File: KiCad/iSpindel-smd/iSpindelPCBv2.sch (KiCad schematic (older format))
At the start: 21 parts, among them J1 PROG, J2 PROG_con, SW1 SW_DPDT_x2, U1 MIC5219-3.3, U2 GY-521, U3 TP4056-shield-6PIN, U4 DS18B20, U5 LoRa_Ra-02, U6 ESP-07S

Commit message: small fix
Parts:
- added SW?: SW_DPDT_x2, KiCadCustomLibs:SK12D07VG3, symbol SW_DPDT_x2
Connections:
- net VCC: now also SW?.1 (A)
- net at SW1.2 (B), U3.3 (OUT+): now also SW?.2 (B)
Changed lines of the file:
@@
 Wire Wire Line
 	10600 1600 10450 1600
+$Comp
+L SW_DPDT_x2 SW?
+U 1 1 5B55F055
+P 8850 4650
+F 0 "SW?" H 8850 4820 50  0000 C CNN
+F 1 "SW_DPDT_x2" H 8850 4450 50  0000 C CNN
+F 2 "KiCadCustomLibs:SK12D07VG3" H 8850 4650 50  0001 C CNN
+F 3 "" H 8850 4650 50  0001 C CNN
+	1    8850 4650
+	1    0    0    -1
+$EndComp
+Wire Wire Line
+	8650 4650 8500 4650
+Wire Wire Line
+	8500 4650 8500 4100
+Connection ~ 8500 4100
+$Comp
+L VCC #PWR?
+U 1 1 5B55F1C0
+P 9050 4550
+F 0 "#PWR?" H 9050 4400 50  0001 C CNN
+F 1 "VCC" H 9050 4700 50  0000 C CNN
+F 2 "" H 9050 4550 50  0001 C CNN
+F 3 "" H 9050 4550 50  0001 C CNN
+	1    9050 4550
+	1    0    0    -1
+$EndComp
 $EndSCHEMATC

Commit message: Some work still in progress
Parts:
- removed SW1, SW?: SW_DPDT_x2, KiCadCustomLibs:SK12D07VG3, symbol SW_DPDT_x2
- added SW1: SW_SPDT, KiCadCustomLibs:SK12D07VG3, symbol SW_SPDT
- D1: footprint (none) -> Diodes_SMD:D_SOD-523
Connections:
- net VCC: now also SW1.2 (B); no longer J2.4 (Pin_4)
- net at U3.3 (OUT+): now also SW1.3 (C)
- new net VCC_PROG: J2.4 (Pin_4), SW1.1 (A)
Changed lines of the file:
@@
-$EndComp
-$Comp
-L SW_DPDT_x2 SW1
-U 1 1 5B533766
-P 8850 4100
-F 0 "SW1" H 8850 4270 50  0000 C CNN
-F 1 "SW_DPDT_x2" H 8850 3900 50  0000 C CNN
-F 2 "KiCadCustomLibs:SK12D07VG3" H 8850 4100 50  0001 C CNN
-F 3 "" H 8850 4100 50  0001 C CNN
-	1    8850 4100
-	1    0    0    -1
 $EndComp
 $Comp
@@
 	1    0    0    -1
 $EndComp
-Wire Wire Line
-	7850 4100 8650 4100
 NoConn ~ 6850 4100
 NoConn ~ 7850 4600
@@
 F 0 "D1" H 7750 2280 50  0000 L CNN
 F 1 "Schottky" H 7600 2350 50  0000 L CNN
-F 2 "" V 7800 2200 50  0001 C CNN
+F 2 "Diodes_SMD:D_SOD-523" V 7800 2200 50  0001 C CNN
 F 3 "" V 7800 2200 50  0001 C CNN
 	1    7800 2200
@@
 	10150 1700 10600 1700
 $Comp
-L VCC #PWR28
-U 1 1 5B54DB80
-P 10450 1600
-F 0 "#PWR28" H 10450 1450 50  0001 C CNN
-F 1 "VCC" H 10450 1750 50  0000 C CNN
-F 2 "" H 10450 1600 50  0001 C CNN
-F 3 "" H 10450 1600 50  0001 C CNN
-	1    10450 1600
-	1    0    0    -1
-$EndComp
-Wire Wire Line
-	10600 1600 10450 1600
-$Comp
-L SW_DPDT_x2 SW?
-U 1 1 5B55F055
-P 8850 4650
-F 0 "SW?" H 8850 4820 50  0000 C CNN
-F 1 "SW_DPDT_x2" H 8850 4450 50  0000 C CNN
-F 2 "KiCadCustomLibs:SK12D07VG3" H 8850 4650 50  0001 C CNN
-F 3 "" H 8850 4650 50  0001 C CNN
-	1    8850 4650
-	1    0    0    -1
-$EndComp
-Wire Wire Line
-	8650 4650 8500 4650
-Wire Wire Line
-	8500 4650 8500 4100
-Connection ~ 8500 4100
-$Comp
-L VCC #PWR?
-U 1 1 5B55F1C0
-P 9050 4550
-F 0 "#PWR?" H 9050 4400 50  0001 C CNN
-F 1 "VCC" H 9050 4700 50  0000 C CNN
-F 2 "" H 9050 4550 50  0001 C CNN
-F 3 "" H 9050 4550 50  0001 C CNN
-	1    9050 4550
-	1    0    0    -1
-$EndComp
+L SW_SPDT SW1
+U 1 1 5B570E68
+P 8850 4000
+F 0 "SW1" H 8850 4170 50  0000 C CNN
+F 1 "SW_SPDT" H 8850 3800 50  0000 C CNN
+F 2 "KiCadCustomLibs:SK12D07VG3" H 8850 4000 50  0001 C CNN
+F 3 "" H 8850 4000 50  0001 C CNN
+	1    8850 4000
+	-1   0    0    1
+$EndComp
+Text Label 8200 4100 0    60   ~ 0
+VCC_PROG
+Wire Wire Line
+	10600 1600 10150 1600
+Text Label 10150 1600 0    60   ~ 0
+VCC_PROG
+Wire Wire Line
+	7850 4100 7900 4100
+Wire Wire Line
+	7900 4100 7900 3900
+Wire Wire Line
+	7900 3900 8650 3900
+Wire Wire Line
+	8650 4100 8200 4100
 $EndSCHEMATC

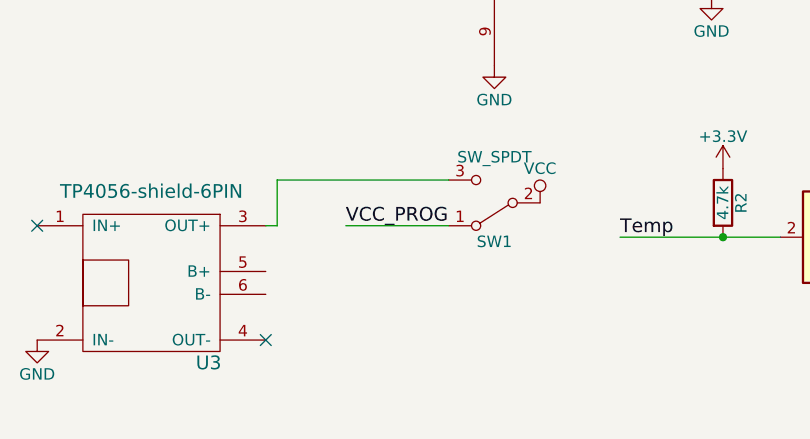
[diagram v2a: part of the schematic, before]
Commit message: Add TH variant
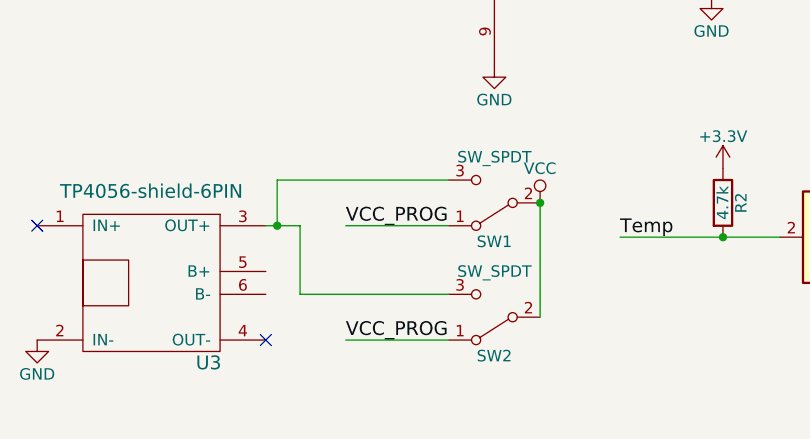
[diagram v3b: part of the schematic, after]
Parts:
- added SW2: SW_SPDT, KiCadCustomLibs:SS-12F23, symbol SW_SPDT
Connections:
- net VCC: now also SW2.2 (B)
- net VCC_PROG: now also SW2.1 (A)
- net at SW1.3 (C), U3.3 (OUT+): now also SW2.3 (C)
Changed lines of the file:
@@
 $EndComp
 $Comp
-L GND #PWR29
+L GND #PWR28
 U 1 1 5B54D95D
 P 10600 1900
-F 0 "#PWR29" H 10600 1650 50  0001 C CNN
+F 0 "#PWR28" H 10600 1650 50  0001 C CNN
 F 1 "GND" H 10600 1750 50  0000 C CNN
 F 2 "" H 10600 1900 50  0001 C CNN
@@
 VCC_PROG
 Wire Wire Line
-	7850 4100 7900 4100
+	7850 4100 8000 4100
 Wire Wire Line
 	7900 4100 7900 3900
@@
 Wire Wire Line
 	8650 4100 8200 4100
+$Comp
+L SW_SPDT SW2
+U 1 1 5B585D1D
+P 8850 4500
+F 0 "SW2" H 8850 4670 50  0000 C CNN
+F 1 "SW_SPDT" H 8850 4300 50  0000 C CNN
+F 2 "KiCadCustomLibs:SS-12F23" H 8850 4500 50  0001 C CNN
+F 3 "" H 8850 4500 50  0001 C CNN
+	1    8850 4500
+	-1   0    0    1
+$EndComp
+Wire Wire Line
+	9050 4000 9050 4500
+Connection ~ 9050 4000
+Wire Wire Line
+	8650 4400 8000 4400
+Wire Wire Line
+	8000 4400 8000 4100
+Connection ~ 7900 4100
+Wire Wire Line
+	8650 4600 8200 4600
+Text Label 8200 4600 0    60   ~ 0
+VCC_PROG
 $EndSCHEMATC

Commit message: Add led
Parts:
- added C6: 100n, Capacitors_SMD:C_0603, symbol C
- added D2: LED, LEDs:LED_0805, symbol LED
- added R7: 4.7k, Resistors_SMD:R_0603, symbol R
- added SW3: SW_Push, KiCadCustomLibs:Button_TS-018, symbol SW_Push
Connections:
- net +3V3: now also R7.1
- net GND: now also C6.2, SW3.2
- net at D1.2 (A), R5.2, U6.1 (REST): now also C6.1, SW3.1
- net LED: now reaches U6.13 (GPIO4)
- net LED: now also D2.1 (K)
- new net: D2.2 (A), R7.2
- no-connect marks 13 -> 12
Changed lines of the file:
@@
 	9400 4150 10100 4150
 $Comp
-L +3.3V #PWR25
+L +3.3V #PWR27
 U 1 1 5B5302EE
 P 9850 3850
-F 0 "#PWR25" H 9850 3700 50  0001 C CNN
+F 0 "#PWR27" H 9850 3700 50  0001 C CNN
 F 1 "+3.3V" H 9850 3990 50  0000 C CNN
 F 2 "" H 9850 3850 50  0001 C CNN
@@
 Connection ~ 9850 4150
 $Comp
-L GND #PWR27
+L GND #PWR29
 U 1 1 5B530B26
 P 10400 4450
-F 0 "#PWR27" H 10400 4200 50  0001 C CNN
+F 0 "#PWR29" H 10400 4200 50  0001 C CNN
 F 1 "GND" H 10400 4300 50  0000 C CNN
 F 2 "" H 10400 4450 50  0001 C CNN
@@
 $EndComp
 $Comp
-L VCC #PWR22
+L VCC #PWR24
 U 1 1 5B53B586
 P 9050 4000
-F 0 "#PWR22" H 9050 3850 50  0001 C CNN
+F 0 "#PWR24" H 9050 3850 50  0001 C CNN
 F 1 "VCC" H 9050 4150 50  0000 C CNN
 F 2 "" H 9050 4000 50  0001 C CNN
@@
 $EndComp
 $Comp
-L VCC #PWR26
+L VCC #PWR28
 U 1 1 5B53B686
 P 10400 3850
-F 0 "#PWR26" H 10400 3700 50  0001 C CNN
+F 0 "#PWR28" H 10400 3700 50  0001 C CNN
 F 1 "VCC" H 10400 4000 50  0000 C CNN
 F 2 "" H 10400 3850 50  0001 C CNN
@@
 	7450 2300 7950 2300
 $Comp
-L GND #PWR16
+L GND #PWR17
 U 1 1 5B542A93
 P 7450 2600
-F 0 "#PWR16" H 7450 2350 50  0001 C CNN
+F 0 "#PWR17" H 7450 2350 50  0001 C CNN
 F 1 "GND" H 7450 2450 50  0000 C CNN
 F 2 "" H 7450 2600 50  0001 C CNN
@@
 $EndComp
 $Comp
-L VCC #PWR15
+L VCC #PWR16
 U 1 1 5B542B16
 P 7450 2000
-F 0 "#PWR15" H 7450 1850 50  0001 C CNN
+F 0 "#PWR16" H 7450 1850 50  0001 C CNN
 F 1 "VCC" H 7450 2150 50  0000 C CNN
 F 2 "" H 7450 2000 50  0001 C CNN
@@
 Connection ~ 7450 2300
 $Comp
-L +3.3V #PWR20
+L +3.3V #PWR22
 U 1 1 5B542EA1
 P 8850 1600
-F 0 "#PWR20" H 8850 1450 50  0001 C CNN
+F 0 "#PWR22" H 8850 1450 50  0001 C CNN
 F 1 "+3.3V" H 8850 1740 50  0000 C CNN
 F 2 "" H 8850 1600 50  0001 C CNN
@@
 $EndComp
 $Comp
-L GND #PWR21
+L GND #PWR23
 U 1 1 5B54787D
 P 8850 3400
-F 0 "#PWR21" H 8850 3150 50  0001 C CNN
+F 0 "#PWR23" H 8850 3150 50  0001 C CNN
 F 1 "GND" H 8850 3250 50  0000 C CNN
 F 2 "" H 8850 3400 50  0001 C CNN
@@
 P 7800 2200
 F 0 "D1" H 7750 2280 50  0000 L CNN
-F 1 "Schottky" H 7600 2350 50  0000 L CNN
+F 1 "Schottky" H 7550 2350 50  0001 L CNN
 F 2 "Diodes_SMD:D_SOD-523" V 7800 2200 50  0001 C CNN
 F 3 "" V 7800 2200 50  0001 C CNN
@@
 Text Label 7650 2600 0    60   ~ 0
 SCK
-NoConn ~ 9750 2500
 Wire Wire Line
 	7950 2400 7800 2400
@@
 $EndComp
 $Comp
-L +3.3V #PWR17
+L +3.3V #PWR19
 U 1 1 5B548D3F
 P 7950 1750
-F 0 "#PWR17" H 7950 1600 50  0001 C CNN
+F 0 "#PWR19" H 7950 1600 50  0001 C CNN
 F 1 "+3.3V" H 7950 1890 50  0000 C CNN
 F 2 "" H 7950 1750 50  0001 C CNN
@@
 Connection ~ 9800 2800
 $Comp
-L GND #PWR23
+L GND #PWR25
 U 1 1 5B549B49
 P 9800 3100
-F 0 "#PWR23" H 9800 2850 50  0001 C CNN
+F 0 "#PWR25" H 9800 2850 50  0001 C CNN
 F 1 "GND" H 9800 2950 50  0000 C CNN
 F 2 "" H 9800 3100 50  0001 C CNN
@@
 	8250 1250 8500 1250
 $Comp
-L +3.3V #PWR18
+L +3.3V #PWR20
 U 1 1 5B54A171
 P 8400 1250
-F 0 "#PWR18" H 8400 1100 50  0001 C CNN
+F 0 "#PWR20" H 8400 1100 50  0001 C CNN
 F 1 "+3.3V" H 8400 1390 50  0000 C CNN
 F 2 "" H 8400 1250 50  0001 C CNN
@@
 Connection ~ 8400 1250
 $Comp
-L GND #PWR19
+L GND #PWR21
 U 1 1 5B54A232
 P 8400 1550
-F 0 "#PWR19" H 8400 1300 50  0001 C CNN
+F 0 "#PWR21" H 8400 1300 50  0001 C CNN
 F 1 "GND" H 8400 1400 50  0000 C CNN
 F 2 "" H 8400 1550 50  0001 C CNN
@@
 SDA
 $Comp
-L GND #PWR24
+L GND #PWR26
 U 1 1 5B54AE12
 P 9850 1550
-F 0 "#PWR24" H 9850 1300 50  0001 C CNN
+F 0 "#PWR26" H 9850 1300 50  0001 C CNN
 F 1 "GND" H 9850 1400 50  0000 C CNN
 F 2 "" H 9850 1550 50  0001 C CNN
@@
 $EndComp
 $Comp
-L GND #PWR28
+L GND #PWR30
 U 1 1 5B54D95D
 P 10600 1900
-F 0 "#PWR28" H 10600 1650 50  0001 C CNN
+F 0 "#PWR30" H 10600 1650 50  0001 C CNN
 F 1 "GND" H 10600 1750 50  0000 C CNN
 F 2 "" H 10600 1900 50  0001 C CNN
@@
 Text Label 8200 4600 0    60   ~ 0
 VCC_PROG
+$Comp
+L SW_Push SW3
+U 1 1 5B5AFB9B
+P 7350 1600
+F 0 "SW3" H 7400 1700 50  0000 L CNN
+F 1 "SW_Push" H 7350 1540 50  0000 C CNN
+F 2 "KiCadCustomLibs:Button_TS-018" H 7350 1800 50  0001 C CNN
+F 3 "" H 7350 1800 50  0001 C CNN
+	1    7350 1600
+	-1   0    0    -1
+$EndComp
+Wire Wire Line
+	7550 1600 7750 1600
+Wire Wire Line
+	7750 1600 7750 2050
+Wire Wire Line
+	7750 2050 7950 2050
+Connection ~ 7950 2050
+$Comp
+L GND #PWR15
+U 1 1 5B5AFCF8
+P 7150 1700
+F 0 "#PWR15" H 7150 1450 50  0001 C CNN
+F 1 "GND" H 7150 1550 50  0000 C CNN
+F 2 "" H 7150 1700 50  0001 C CNN
+F 3 "" H 7150 1700 50  0001 C CNN
+	1    7150 1700
+	1    0    0    -1
+$EndComp
+Wire Wire Line
+	7150 1600 7150 1700
+$Comp
+L C C6
+U 1 1 5B5B067E
+P 7600 1750
+F 0 "C6" H 7625 1850 50  0000 L CNN
+F 1 "100n" H 7600 1950 50  0000 L CNN
+F 2 "Capacitors_SMD:C_0603" H 7638 1600 50  0001 C CNN
+F 3 "" H 7600 1750 50  0001 C CNN
+	1    7600 1750
+	1    0    0    -1
+$EndComp
+Connection ~ 7600 1600
+$Comp
+L GND #PWR18
+U 1 1 5B5B0740
+P 7600 1900
+F 0 "#PWR18" H 7600 1650 50  0001 C CNN
+F 1 "GND" H 7600 1750 50  0000 C CNN
+F 2 "" H 7600 1900 50  0001 C CNN
+F 3 "" H 7600 1900 50  0001 C CNN
+	1    7600 1900
+	1    0    0    -1
+$EndComp
+Wire Wire Line
+	9750 2500 10050 2500
+Text Label 10050 2500 2    60   ~ 0
+LED
+$Comp
+L LED D2
+U 1 1 5B5B3D9A
+P 10400 3150
+F 0 "D2" H 10400 3250 50  0000 C CNN
+F 1 "LED" H 10400 3050 50  0000 C CNN
+F 2 "LEDs:LED_0805" H 10400 3150 50  0001 C CNN
+F 3 "" H 10400 3150 50  0001 C CNN
+	1    10400 3150
+	1    0    0    -1
+$EndComp
+$Comp
+L R R7
+U 1 1 5B5B4294
+P 10700 3150
+F 0 "R7" V 10780 3150 50  0000 C CNN
+F 1 "4.7k" V 10700 3150 50  0000 C CNN
+F 2 "Resistors_SMD:R_0603" V 10630 3150 50  0001 C CNN
+F 3 "" H 10700 3150 50  0001 C CNN
+	1    10700 3150
+	0    1    1    0
+$EndComp
+$Comp
+L +3.3V #PWR31
+U 1 1 5B5B4324
+P 10850 3150
+F 0 "#PWR31" H 10850 3000 50  0001 C CNN
+F 1 "+3.3V" H 10850 3290 50  0000 C CNN
+F 2 "" H 10850 3150 50  0001 C CNN
+F 3 "" H 10850 3150 50  0001 C CNN
+	1    10850 3150
+	1    0    0    -1
+$EndComp
+Wire Wire Line
+	10250 3150 10000 3150
+Text Label 10000 3150 0    60   ~ 0
+LED
 $EndSCHEMATC

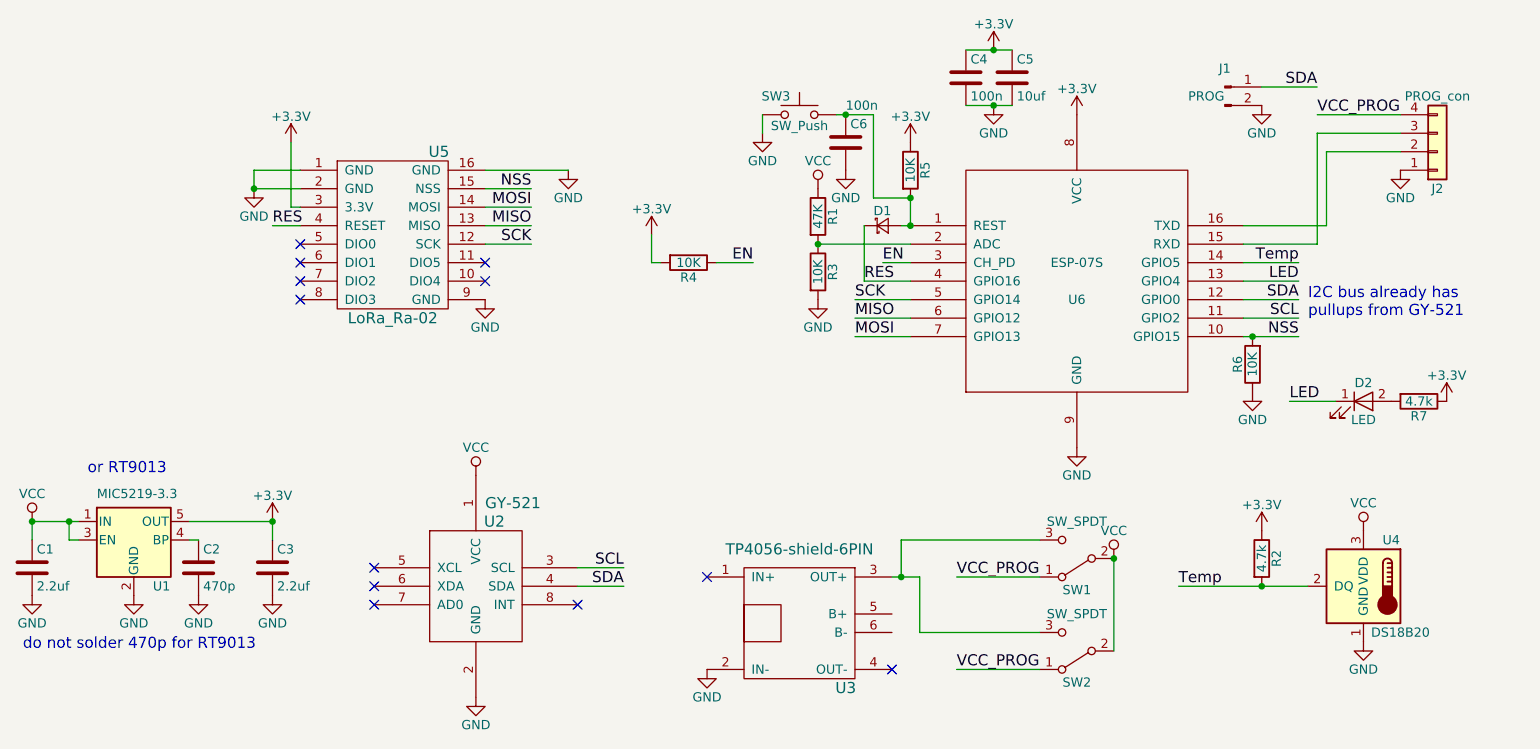
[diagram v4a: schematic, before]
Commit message: Some minor adjustments to PCB. Added capacitor to DS
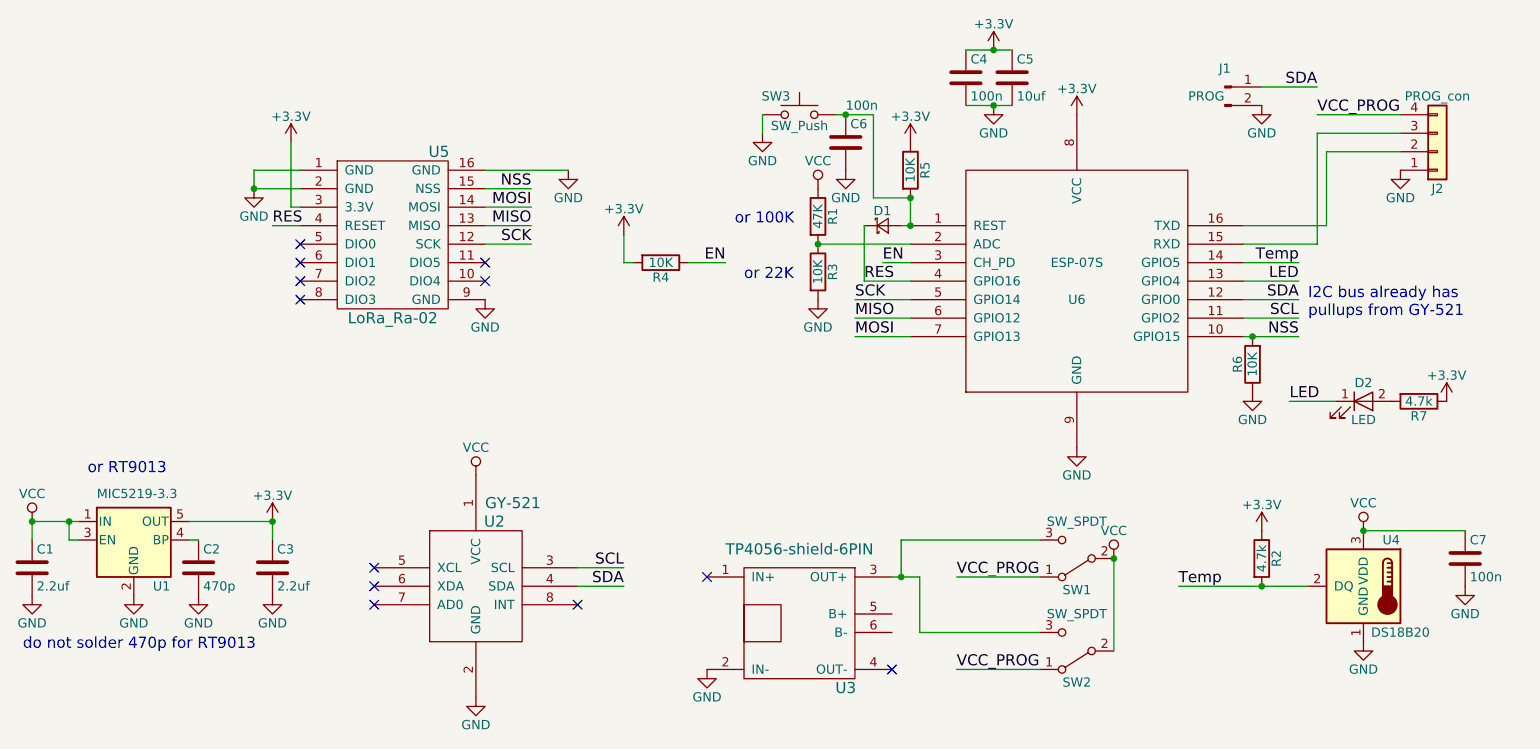
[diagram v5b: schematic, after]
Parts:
- added C7: 100n, Capacitors_SMD:C_0603, symbol C
- D1: footprint Diodes_SMD:D_SOD-523 -> Diodes_SMD:D_SOD-323
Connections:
- net GND: now also C7.2
- net VCC: now also C7.1
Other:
- note added: "or 100K"
- note added: "or 22K"
- moved on the sheet: R4
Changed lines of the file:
@@
 F 0 "D1" H 7750 2280 50  0000 L CNN
 F 1 "Schottky" H 7550 2350 50  0001 L CNN
-F 2 "Diodes_SMD:D_SOD-523" V 7800 2200 50  0001 C CNN
+F 2 "Diodes_SMD:D_SOD-323" V 7800 2200 50  0001 C CNN
 F 3 "" V 7800 2200 50  0001 C CNN
 	1    7800 2200
@@
 L R R4
 U 1 1 5B548C3F
-P 6750 2400
-F 0 "R4" V 6830 2400 50  0000 C CNN
-F 1 "10K" V 6750 2400 50  0000 C CNN
-F 2 "Resistors_SMD:R_0603" V 6680 2400 50  0001 C CNN
-F 3 "" H 6750 2400 50  0001 C CNN
-	1    6750 2400
+P 6600 2400
+F 0 "R4" V 6680 2400 50  0000 C CNN
+F 1 "10K" V 6600 2400 50  0000 C CNN
+F 2 "Resistors_SMD:R_0603" V 6530 2400 50  0001 C CNN
+F 3 "" H 6600 2400 50  0001 C CNN
+	1    6600 2400
 	0    1    1    0
 $EndComp
@@
 	7700 2500 7700 2200
 Wire Wire Line
-	6900 2400 7100 2400
-Text Label 7100 2400 2    60   ~ 0
+	6750 2400 6950 2400
+Text Label 6950 2400 2    60   ~ 0
 EN
 $Comp
 L +3.3V #PWR13
 U 1 1 5B5490C2
-P 6550 2250
-F 0 "#PWR13" H 6550 2100 50  0001 C CNN
-F 1 "+3.3V" H 6550 2390 50  0000 C CNN
-F 2 "" H 6550 2250 50  0001 C CNN
-F 3 "" H 6550 2250 50  0001 C CNN
-	1    6550 2250
+P 6400 2250
+F 0 "#PWR13" H 6400 2100 50  0001 C CNN
+F 1 "+3.3V" H 6400 2390 50  0000 C CNN
+F 2 "" H 6400 2250 50  0001 C CNN
+F 3 "" H 6400 2250 50  0001 C CNN
+	1    6400 2250
 	1    0    0    -1
 $EndComp
@@
 I2C bus already has \npullups from GY-521
 Wire Wire Line
-	6600 2400 6550 2400
-Wire Wire Line
-	6550 2400 6550 2250
+	6450 2400 6400 2400
+Wire Wire Line
+	6400 2400 6400 2250
 Connection ~ 9800 2800
 $Comp
@@
 Text Label 10000 3150 0    60   ~ 0
 LED
+Text Notes 7000 2200 0    60   ~ 0
+or 100K
+Text Notes 7050 2500 0    60   ~ 0
+or 22K
+$Comp
+L C C7
+U 1 1 5B741712
+P 10950 4000
+F 0 "C7" H 10975 4100 50  0000 L CNN
+F 1 "100n" H 10975 3900 50  0000 L CNN
+F 2 "Capacitors_SMD:C_0603" H 10988 3850 50  0001 C CNN
+F 3 "" H 10950 4000 50  0001 C CNN
+	1    10950 4000
+	1    0    0    -1
+$EndComp
+Wire Wire Line
+	10400 3850 10950 3850
+$Comp
+L GND #PWR32
+U 1 1 5B741CDF
+P 10950 4150
+F 0 "#PWR32" H 10950 3900 50  0001 C CNN
+F 1 "GND" H 10950 4000 50  0000 C CNN
+F 2 "" H 10950 4150 50  0001 C CNN
+F 3 "" H 10950 4150 50  0001 C CNN
+	1    10950 4150
+	1    0    0    -1
+$EndComp
+Connection ~ 10400 3850
 $EndSCHEMATC
